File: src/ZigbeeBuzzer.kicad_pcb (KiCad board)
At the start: 2 copper layers, 26 x 21 mm, 12 parts, among them Q1 NPN, U1 Xiao-ESP32-C6

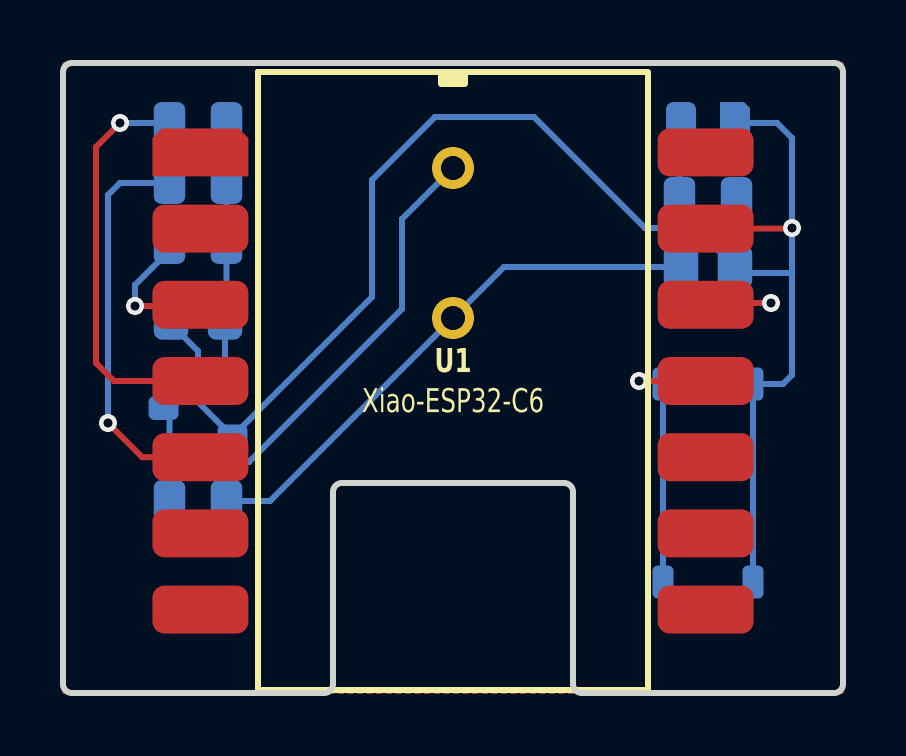
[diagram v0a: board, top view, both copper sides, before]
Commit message: Added 3V3 voltage divider
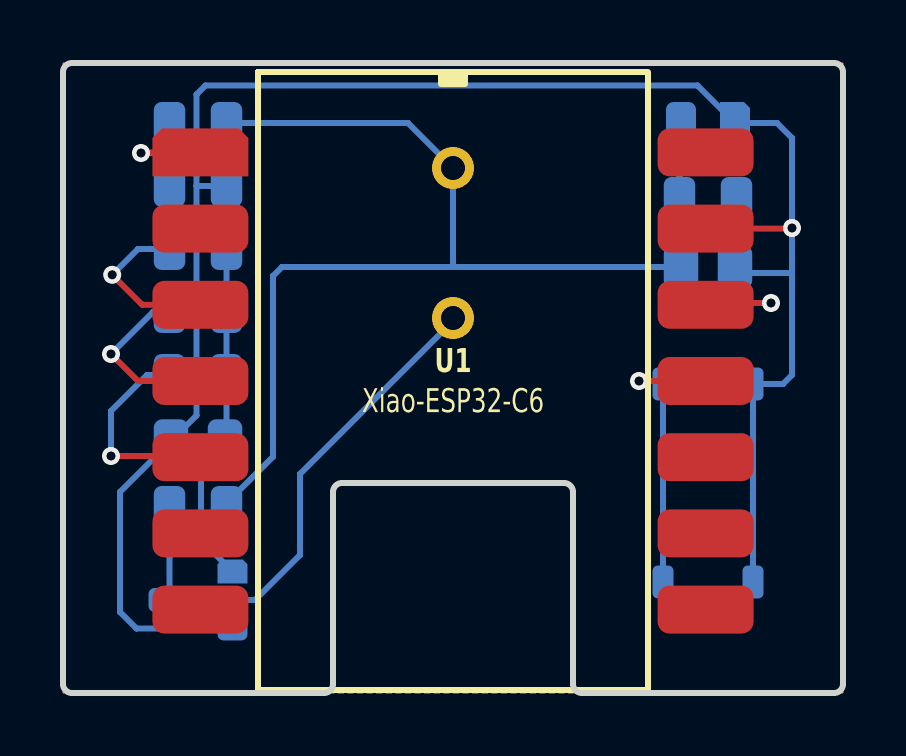
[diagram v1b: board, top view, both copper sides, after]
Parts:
- added R7: 100K, Medo64:R (0805), B.Cu at (24.5, 22.0)
- added R8: 100K, Medo64:R (0805), B.Cu at (24.5, 24.1)
- moved Q1 6.40 mm to (24.5, 37.9)
- moved R1 4.40 mm to (24.5, 30.4)
- moved R2 4.30 mm to (24.5, 28.3)
- moved R5 4.20 mm to (24.5, 26.2)
- moved C1 4.10 mm to (24.5, 32.6)
- moved R3 0.20 mm to (24.5, 34.8)
- turned LS1 to -90 degrees
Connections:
- R1 pad 1: PWM1 -> PWM3
- R2 pad 1: PWM3 -> PWM2
- R5 pad 1: PWM2 -> PWM1
- U1 pad 1: (no net) -> ADC
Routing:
- net 3V3: track 24.7 -> 39.7 mm
- net GND: track 53.7 -> 65.3 mm
- net PWM2: track 14.5 -> 6.68 mm
- net PWM3: track 14.2 -> 7.69 mm
- net ADC: track 0.00 -> 5.86 mm, vias 0 -> 1
- net BASE: track 8.25 -> 11.6 mm
- net PWM1: track 3.23 -> 6.42 mm
